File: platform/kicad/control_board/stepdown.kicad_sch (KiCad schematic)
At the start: 7 parts, among them U1 AP63205WU-7

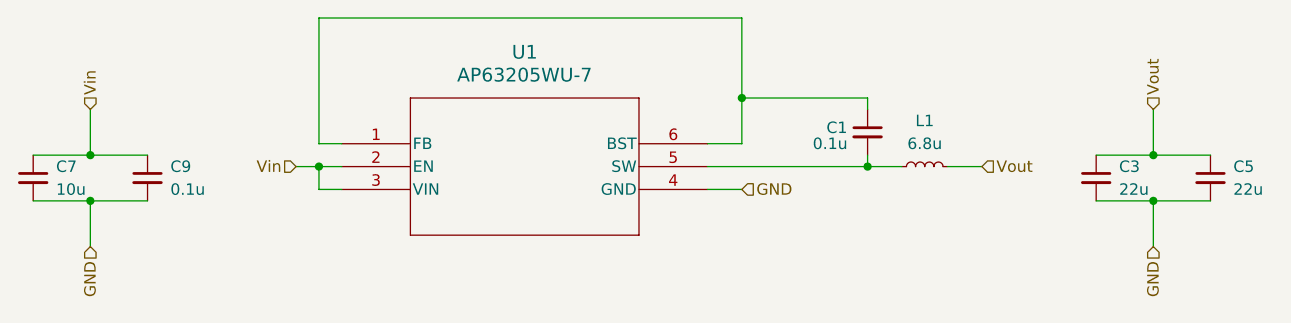
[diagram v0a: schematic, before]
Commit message: Control PCB: Update layout (#3)
This change updates the layout of the PCB to revise the feedback from the previous iteration.
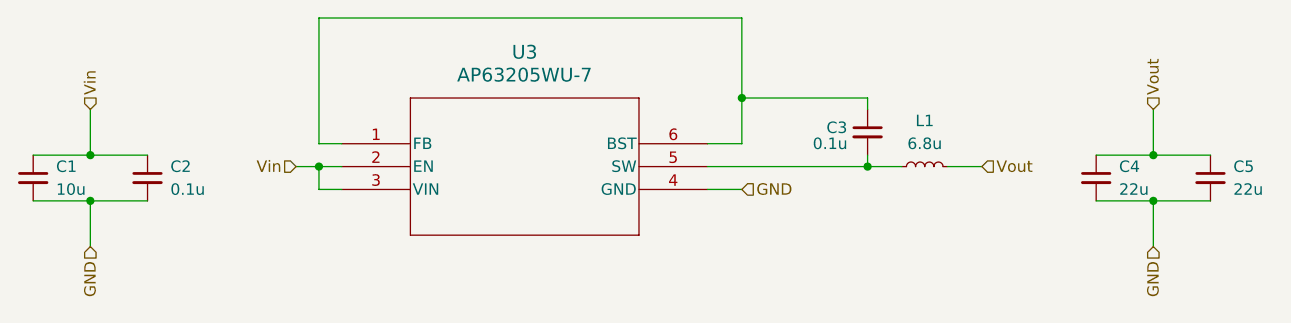
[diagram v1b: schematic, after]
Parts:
- renumbered C7 to C1, C9 to C2, C1 to C3, C3 to C4, U1 to U3
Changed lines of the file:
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@@
 		(on_board yes)
 		(dnp no)
-		(property "Reference" "C1"
+		(property "Reference" "C3"
 			(at 174.498 90.932 0)
 			(effects
@@
 			(project ""
 				(path "/bacab6d6-2a0b-4208-9256-c826bcae29b3/0626e775-86df-4156-8b81-537b056df5a8"
-					(reference "C1")
+					(reference "C3")
 					(unit 1)
 				)
@@
 		(dnp no)
 		(fields_autoplaced yes)
-		(property "Reference" "U1"
+		(property "Reference" "U3"
 			(at 140.97 82.55 0)
 			(effects
@@
 			(project ""
 				(path "/bacab6d6-2a0b-4208-9256-c826bcae29b3/0626e775-86df-4156-8b81-537b056df5a8"
-					(reference "U1")
+					(reference "U3")
 					(unit 1)
 				)
@@
 		(dnp no)
 		(fields_autoplaced yes)
-		(property "Reference" "C3"
+		(property "Reference" "C4"
 			(at 207.01 95.2562 0)
 			(effects
@@
 			(project "control_board"
 				(path "/bacab6d6-2a0b-4208-9256-c826bcae29b3/0626e775-86df-4156-8b81-537b056df5a8"
-					(reference "C3")
+					(reference "C4")
 					(unit 1)
 				)
@@
 		(dnp no)
 		(fields_autoplaced yes)
-		(property "Reference" "C7"
+		(property "Reference" "C1"
 			(at 88.9 95.2562 0)
 			(effects
@@
 			(project "control_board"
 				(path "/bacab6d6-2a0b-4208-9256-c826bcae29b3/0626e775-86df-4156-8b81-537b056df5a8"
-					(reference "C7")
+					(reference "C1")
 					(unit 1)
 				)
@@
 		(dnp no)
 		(fields_autoplaced yes)
-		(property "Reference" "C9"
+		(property "Reference" "C2"
 			(at 101.6 95.2562 0)
 			(effects
@@
 			(project "control_board"
 				(path "/bacab6d6-2a0b-4208-9256-c826bcae29b3/0626e775-86df-4156-8b81-537b056df5a8"
-					(reference "C9")
-					(unit 1)
-				)
+					(reference "C2")
+					(unit 1)
+				)

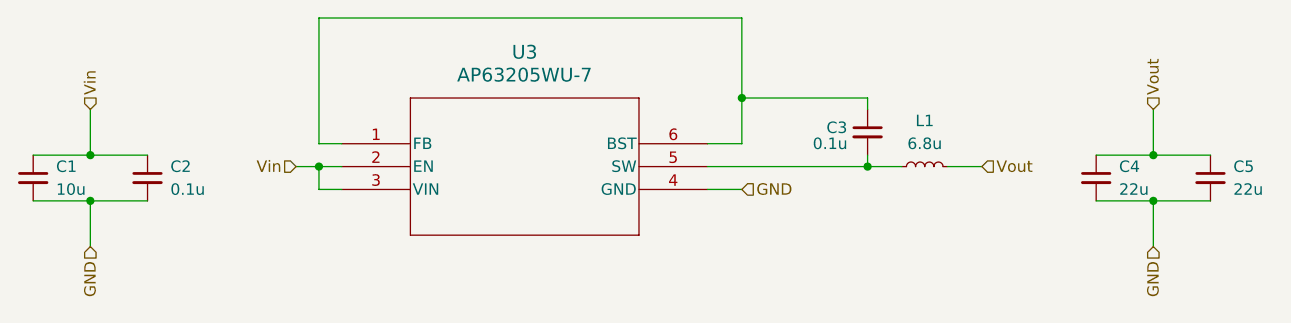
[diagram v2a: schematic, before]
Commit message: Peripheral PCB: Initial schematic and layout
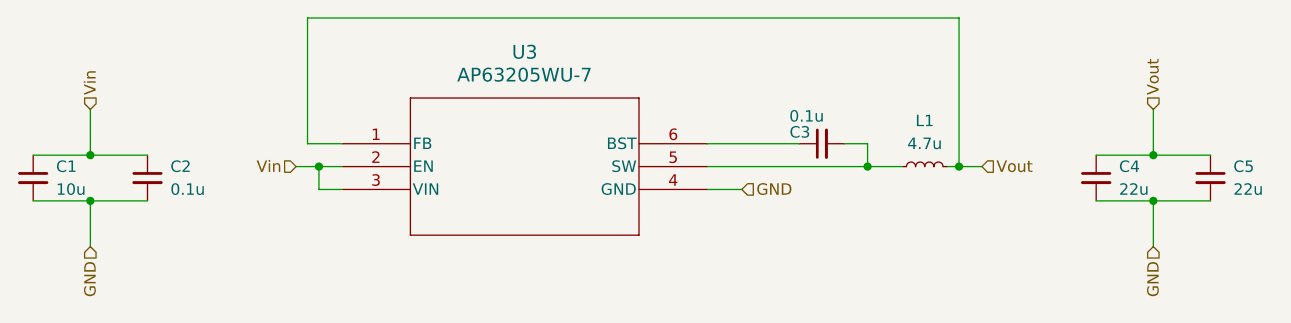
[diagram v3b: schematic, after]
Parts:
- L1: value 6.8u -> 4.7u
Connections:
- net Vout: now also U3.1 (FB)
- net at C3.1, U3.6 (BST): no longer U3.1 (FB)
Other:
- moved on the sheet: C3
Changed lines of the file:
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@@
-	)
-	(junction
-		(at 165.1 87.63)
-		(diameter 0)
-		(color 0 0 0 0)
 	)
 	(junction
@@
 	)
 	(junction
+		(at 189.23 95.25)
+		(diameter 0)
+		(color 0 0 0 0)
+	)
+	(junction
 		(at 210.82 93.98)
 		(diameter 0)
@@
 	(wire
 		(pts
-			(xy 165.1 87.63) (xy 179.07 87.63)
+			(xy 176.53 92.71) (xy 179.07 92.71)
 		)
 		(stroke
@@
 	(wire
 		(pts
-			(xy 165.1 87.63) (xy 165.1 92.71)
-		)
-		(stroke
-			(width 0)
-			(type default)
-		)
-	)
-	(wire
-		(pts
-			(xy 179.07 93.98) (xy 179.07 95.25)
+			(xy 189.23 95.25) (xy 191.77 95.25)
 		)
 		(stroke
@@
 	(wire
 		(pts
-			(xy 179.07 87.63) (xy 179.07 88.9)
-		)
-		(stroke
-			(width 0)
-			(type default)
-		)
-	)
-	(wire
-		(pts
-			(xy 187.96 95.25) (xy 191.77 95.25)
+			(xy 187.96 95.25) (xy 189.23 95.25)
 		)
 		(stroke
@@
 	(wire
 		(pts
-			(xy 118.11 78.74) (xy 118.11 92.71)
+			(xy 116.84 78.74) (xy 116.84 92.71)
 		)
 		(stroke
@@
 	(wire
 		(pts
-			(xy 165.1 78.74) (xy 118.11 78.74)
-		)
-		(stroke
-			(width 0)
-			(type default)
-		)
-	)
-	(wire
-		(pts
-			(xy 161.29 92.71) (xy 165.1 92.71)
+			(xy 116.84 78.74) (xy 189.23 78.74)
+		)
+		(stroke
+			(width 0)
+			(type default)
+		)
+	)
+	(wire
+		(pts
+			(xy 161.29 92.71) (xy 171.45 92.71)
 		)
 		(stroke
@@
 	(wire
 		(pts
-			(xy 118.11 92.71) (xy 120.65 92.71)
+			(xy 116.84 92.71) (xy 120.65 92.71)
+		)
+		(stroke
+			(width 0)
+			(type default)
+		)
+	)
+	(wire
+		(pts
+			(xy 189.23 78.74) (xy 189.23 95.25)
 		)
 		(stroke
@@
 	(wire
 		(pts
-			(xy 165.1 87.63) (xy 165.1 78.74)
+			(xy 179.07 92.71) (xy 179.07 95.25)
 		)
 		(stroke
@@
 	(symbol
 		(lib_id "Device:C_Small")
-		(at 179.07 91.44 0)
+		(at 173.99 92.71 90)
 		(unit 1)
 		(exclude_from_sim no)
@@
 		(dnp no)
 		(property "Reference" "C3"
-			(at 174.498 90.932 0)
+			(at 172.72 91.44 90)
 			(effects
 				(font
@@
 		)
 		(property "Value" "0.1u"
-			(at 172.974 92.71 0)
+			(at 174.244 89.662 90)
 			(effects
 				(font
@@
 		)
 		(property "Footprint" "Capacitor_SMD:C_0603_1608Metric"
-			(at 179.07 91.44 0)
+			(at 173.99 92.71 0)
 			(effects
 				(font
@@
 		)
 		(property "Datasheet" "~"
-			(at 179.07 91.44 0)
+			(at 173.99 92.71 0)
 			(effects
 				(font
@@
 		)
 		(property "Description" "Unpolarized capacitor, small symbol"
-			(at 179.07 91.44 0)
+			(at 173.99 92.71 0)
 			(effects
 				(font
@@
 		)
 		(instances
+			(project "control_board"
+				(path "/8dfa5814-59de-42fa-a019-7b76c06633d1/ed256e33-7579-48c9-89db-6cd9c2f02edb"
+					(reference "C3")
+					(unit 1)
+				)
+			)
 			(project "control_board"
 				(path "/bacab6d6-2a0b-4208-9256-c826bcae29b3/5c908c9f-4997-4e6c-84f5-82f8ec5dbea2/2651b86c-0fa5-4d3d-bbf0-9f89809a43e2"
@@
 		(instances
 			(project "control_board"
+				(path "/8dfa5814-59de-42fa-a019-7b76c06633d1/ed256e33-7579-48c9-89db-6cd9c2f02edb"
+					(reference "C5")
+					(unit 1)
+				)
+			)
+			(project "control_board"
 				(path "/bacab6d6-2a0b-4208-9256-c826bcae29b3/5c908c9f-4997-4e6c-84f5-82f8ec5dbea2/2651b86c-0fa5-4d3d-bbf0-9f89809a43e2"
 					(reference "C5")
@@
 		(instances
 			(project "control_board"
+				(path "/8dfa5814-59de-42fa-a019-7b76c06633d1/ed256e33-7579-48c9-89db-6cd9c2f02edb"
+					(reference "U3")
+					(unit 1)
+				)
+			)
+			(project "control_board"
 				(path "/bacab6d6-2a0b-4208-9256-c826bcae29b3/5c908c9f-4997-4e6c-84f5-82f8ec5dbea2/2651b86c-0fa5-4d3d-bbf0-9f89809a43e2"
 					(reference "U3")
@@
 			)
 		)
-		(property "Value" "6.8u"
+		(property "Value" "4.7u"
 			(at 185.42 92.71 90)
 			(effects
@@
 		)
 		(instances
+			(project "control_board"
+				(path "/8dfa5814-59de-42fa-a019-7b76c06633d1/ed256e33-7579-48c9-89db-6cd9c2f02edb"
+					(reference "L1")
+					(unit 1)
+				)
+			)
 			(project "control_board"
 				(path "/bacab6d6-2a0b-4208-9256-c826bcae29b3/5c908c9f-4997-4e6c-84f5-82f8ec5dbea2/2651b86c-0fa5-4d3d-bbf0-9f89809a43e2"
@@
 		(instances
 			(project "control_board"
+				(path "/8dfa5814-59de-42fa-a019-7b76c06633d1/ed256e33-7579-48c9-89db-6cd9c2f02edb"
+					(reference "C4")
+					(unit 1)
+				)
+			)
+			(project "control_board"
 				(path "/bacab6d6-2a0b-4208-9256-c826bcae29b3/5c908c9f-4997-4e6c-84f5-82f8ec5dbea2/2651b86c-0fa5-4d3d-bbf0-9f89809a43e2"
 					(reference "C4")
@@
 		(instances
 			(project "control_board"
+				(path "/8dfa5814-59de-42fa-a019-7b76c06633d1/ed256e33-7579-48c9-89db-6cd9c2f02edb"
+					(reference "C1")
+					(unit 1)
+				)
+			)
+			(project "control_board"
 				(path "/bacab6d6-2a0b-4208-9256-c826bcae29b3/5c908c9f-4997-4e6c-84f5-82f8ec5dbea2/2651b86c-0fa5-4d3d-bbf0-9f89809a43e2"
 					(reference "C1")
@@
 		(instances
 			(project "control_board"
+				(path "/8dfa5814-59de-42fa-a019-7b76c06633d1/ed256e33-7579-48c9-89db-6cd9c2f02edb"
+					(reference "C2")
+					(unit 1)
+				)
+			)
+			(project "control_board"
 				(path "/bacab6d6-2a0b-4208-9256-c826bcae29b3/5c908c9f-4997-4e6c-84f5-82f8ec5dbea2/2651b86c-0fa5-4d3d-bbf0-9f89809a43e2"

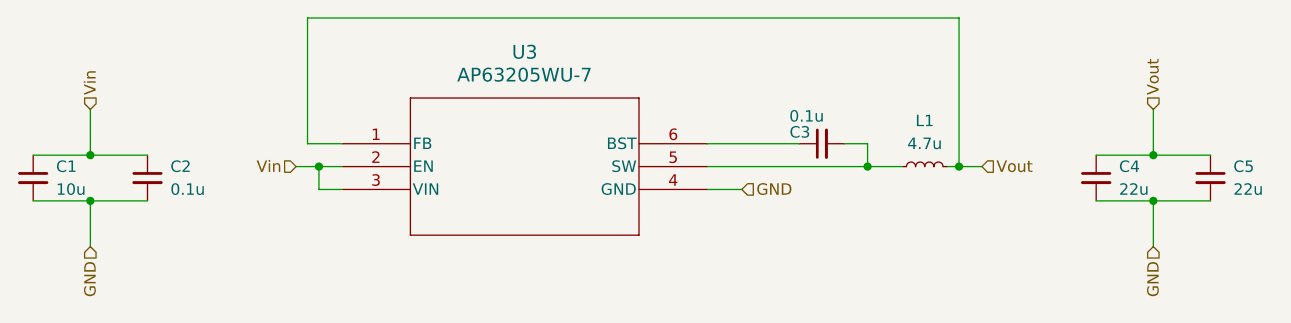
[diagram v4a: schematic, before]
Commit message: Control_PCB v4 revB: Finalised Design
This change updates the controller PCB to a finalised state, only requiring
finishing touches to be made for manufacturing.
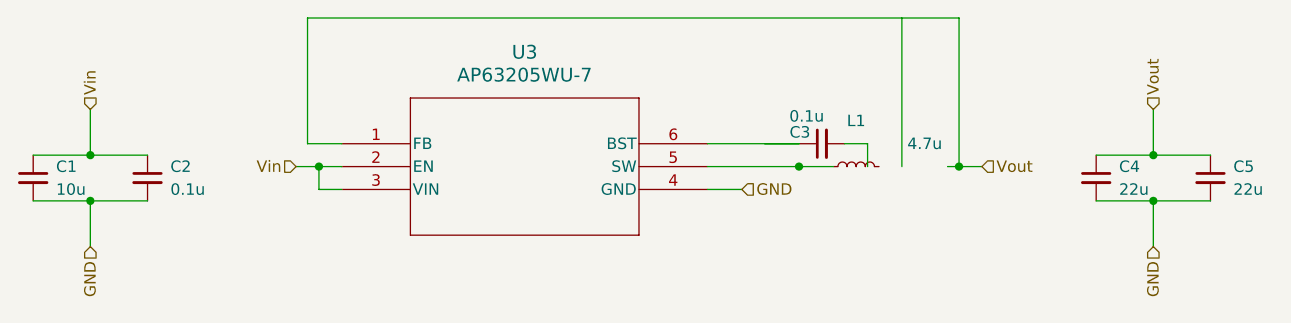
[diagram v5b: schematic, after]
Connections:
- net Vout: no longer L1.2
- net at L1.1, U3.5 (SW): no longer C3.2
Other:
- moved on the sheet: L1
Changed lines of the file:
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@@
 	(paper "A4")
 	(junction
-		(at 179.07 95.25)
+		(at 171.45 95.25)
 		(diameter 0)
 		(color 0 0 0 0)
@@
 	(wire
 		(pts
+			(xy 171.45 95.25) (xy 175.26 95.25)
+		)
+		(stroke
+			(width 0)
+			(type default)
+		)
+	)
+	(wire
+		(pts
+			(xy 182.88 78.74) (xy 182.88 95.25)
+		)
+		(stroke
+			(width 0)
+			(type default)
+		)
+	)
+	(wire
+		(pts
 			(xy 86.36 99.06) (xy 92.71 99.06)
 		)
@@
 	(wire
 		(pts
-			(xy 179.07 95.25) (xy 161.29 95.25)
+			(xy 171.45 95.25) (xy 161.29 95.25)
 		)
 		(stroke
@@
 	(wire
 		(pts
+			(xy 167.64 92.71) (xy 171.45 92.71)
+		)
+		(stroke
+			(width 0)
+			(type default)
+		)
+	)
+	(wire
+		(pts
 			(xy 118.11 97.79) (xy 118.11 95.25)
-		)
-		(stroke
-			(width 0)
-			(type default)
-		)
-	)
-	(wire
-		(pts
-			(xy 179.07 95.25) (xy 182.88 95.25)
 		)
 		(stroke
@@
 		(shape input)
 		(at 210.82 104.14 270)
-		(fields_autoplaced yes)
 		(effects
 			(font
@@
 		(shape input)
 		(at 92.71 104.14 270)
-		(fields_autoplaced yes)
 		(effects
 			(font
@@
 		(shape input)
 		(at 210.82 88.9 90)
-		(fields_autoplaced yes)
 		(effects
 			(font
@@
 		(shape input)
 		(at 165.1 97.79 0)
-		(fields_autoplaced yes)
 		(effects
 			(font
@@
 		(shape input)
 		(at 191.77 95.25 0)
-		(fields_autoplaced yes)
 		(effects
 			(font
@@
 		(shape input)
 		(at 115.57 95.25 180)
-		(fields_autoplaced yes)
 		(effects
 			(font
@@
 		(shape input)
 		(at 92.71 88.9 90)
-		(fields_autoplaced yes)
 		(effects
 			(font
@@
 				(path "/bacab6d6-2a0b-4208-9256-c826bcae29b3/5c908c9f-4997-4e6c-84f5-82f8ec5dbea2/2651b86c-0fa5-4d3d-bbf0-9f89809a43e2"
 					(reference "C3")
+					(unit 1)
+				)
+				(path "/bacab6d6-2a0b-4208-9256-c826bcae29b3/dbf6a82f-5264-47cb-b17a-4f6c5d8ea6fa/a98897ef-202d-4a33-95b8-b01e652c33c4"
+					(reference "C8")
 					(unit 1)
 				)
@@
 					(unit 1)
 				)
+				(path "/bacab6d6-2a0b-4208-9256-c826bcae29b3/dbf6a82f-5264-47cb-b17a-4f6c5d8ea6fa/a98897ef-202d-4a33-95b8-b01e652c33c4"
+					(reference "C10")
+					(unit 1)
+				)
 			)
 		)
@@
 					(unit 1)
 				)
+				(path "/bacab6d6-2a0b-4208-9256-c826bcae29b3/dbf6a82f-5264-47cb-b17a-4f6c5d8ea6fa/a98897ef-202d-4a33-95b8-b01e652c33c4"
+					(reference "U4")
+					(unit 1)
+				)
 			)
 		)
@@
 	(symbol
 		(lib_id "Device:L_Small")
-		(at 185.42 95.25 90)
+		(at 177.8 95.25 90)
 		(unit 1)
 		(exclude_from_sim no)
@@
 		(fields_autoplaced yes)
 		(property "Reference" "L1"
-			(at 185.42 90.17 90)
+			(at 177.8 90.17 90)
 			(effects
 				(font
@@
 		)
 		(property "Footprint" "AusOcean:WE-XHMI_6060"
-			(at 185.42 95.25 0)
+			(at 177.8 95.25 0)
 			(effects
 				(font
@@
 		)
 		(property "Datasheet" "~"
-			(at 185.42 95.25 0)
+			(at 177.8 95.25 0)
 			(effects
 				(font
@@
 		)
 		(property "Description" "Inductor, small symbol"
-			(at 185.42 95.25 0)
+			(at 177.8 95.25 0)
 			(effects
 				(font
@@
 				(path "/bacab6d6-2a0b-4208-9256-c826bcae29b3/5c908c9f-4997-4e6c-84f5-82f8ec5dbea2/2651b86c-0fa5-4d3d-bbf0-9f89809a43e2"
 					(reference "L1")
+					(unit 1)
+				)
+				(path "/bacab6d6-2a0b-4208-9256-c826bcae29b3/dbf6a82f-5264-47cb-b17a-4f6c5d8ea6fa/a98897ef-202d-4a33-95b8-b01e652c33c4"
+					(reference "L2")
 					(unit 1)
 				)
@@
 					(unit 1)
 				)
+				(path "/bacab6d6-2a0b-4208-9256-c826bcae29b3/dbf6a82f-5264-47cb-b17a-4f6c5d8ea6fa/a98897ef-202d-4a33-95b8-b01e652c33c4"
+					(reference "C9")
+					(unit 1)
+				)
 			)
 		)
@@
 					(unit 1)
 				)
+				(path "/bacab6d6-2a0b-4208-9256-c826bcae29b3/dbf6a82f-5264-47cb-b17a-4f6c5d8ea6fa/a98897ef-202d-4a33-95b8-b01e652c33c4"
+					(reference "C6")
+					(unit 1)
+				)
 			)
 		)
@@
 					(unit 1)
 				)
+				(path "/bacab6d6-2a0b-4208-9256-c826bcae29b3/dbf6a82f-5264-47cb-b17a-4f6c5d8ea6fa/a98897ef-202d-4a33-95b8-b01e652c33c4"
+					(reference "C7")
+					(unit 1)
+				)

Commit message: Controller: Finalise for production
This change updates the production files
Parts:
- L1: footprint AusOcean:WE-XHMI_6060 -> Inductor_SMD:L_Changjiang_FXL0630
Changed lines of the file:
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@@
 			)
 		)
-		(property "Footprint" "AusOcean:WE-XHMI_6060"
+		(property "Footprint" "Inductor_SMD:L_Changjiang_FXL0630"
 			(at 177.8 95.25 0)
 			(effects

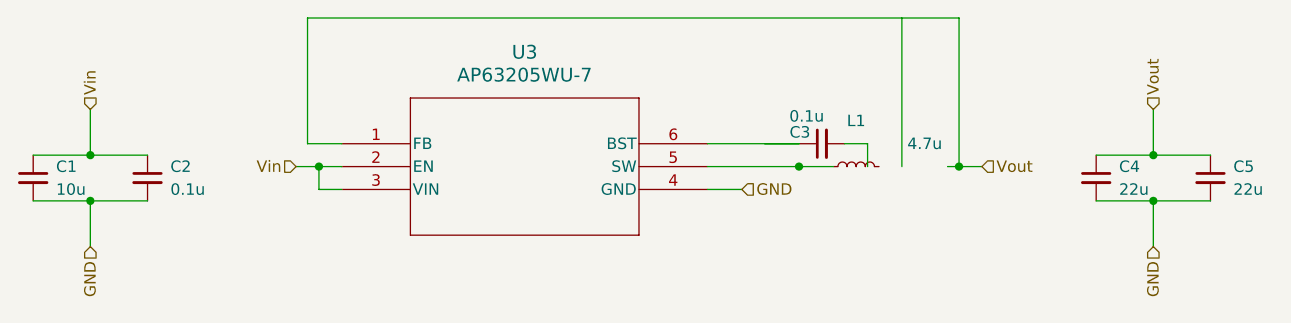
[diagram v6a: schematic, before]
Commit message: Controller: Finalise for production
This change updates the production files
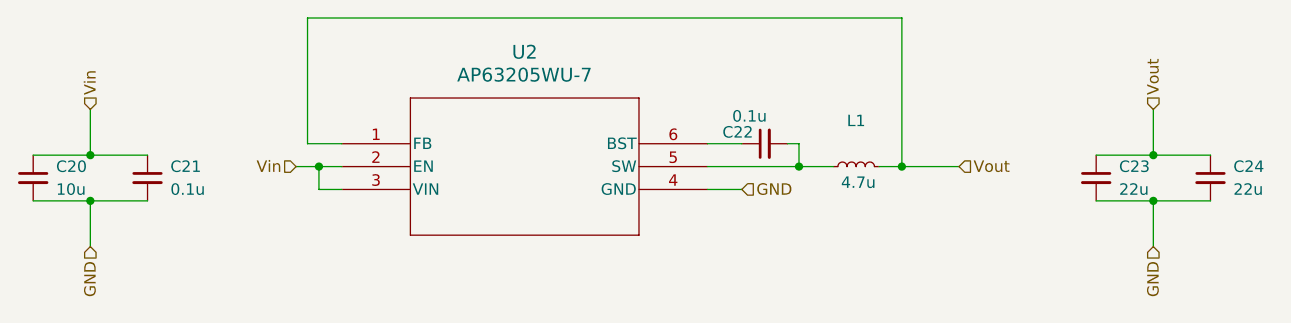
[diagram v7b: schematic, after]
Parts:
- renumbered C1 to C20, C2 to C21, C3 to C22, C4 to C23, C5 to C24, U3 to U2
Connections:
- net Vout: now also L1.2
- net at C22.2: now also L1.1, U2.5 (SW)
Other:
- moved on the sheet: C22
